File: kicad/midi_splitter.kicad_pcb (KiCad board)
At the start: 2 copper layers, 96 x 50 mm, 44 parts, among them J1 DIN-5_180degree, J2 DIN-5_180degree, J3 DIN-5_180degree, J4 DIN-5_180degree, J5 DIN-5_180degree, J6 Barrel_Jack_Switch, J7 DIN-5_180degree, Q1 BC817, U1 6N138, U2 74LS14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

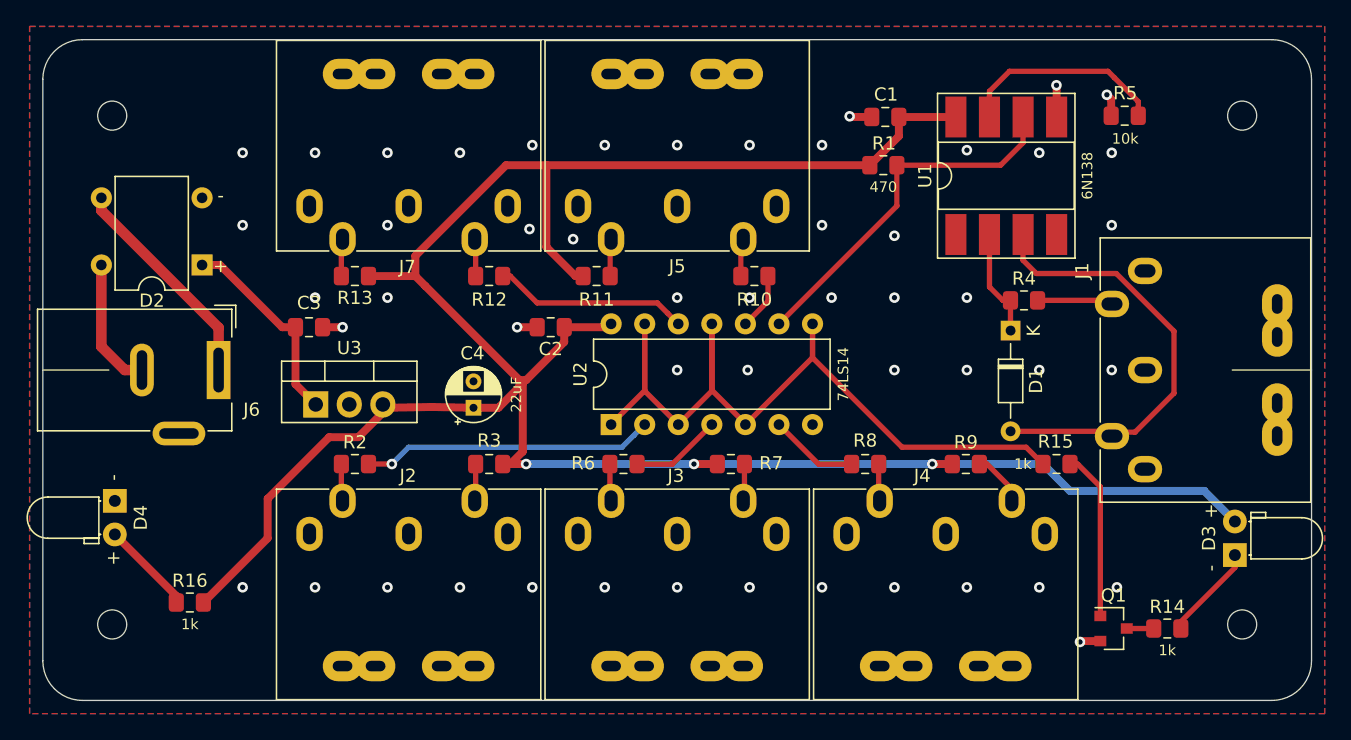
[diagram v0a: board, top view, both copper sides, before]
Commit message: Adding 6th MIDI OUT and USB power input.
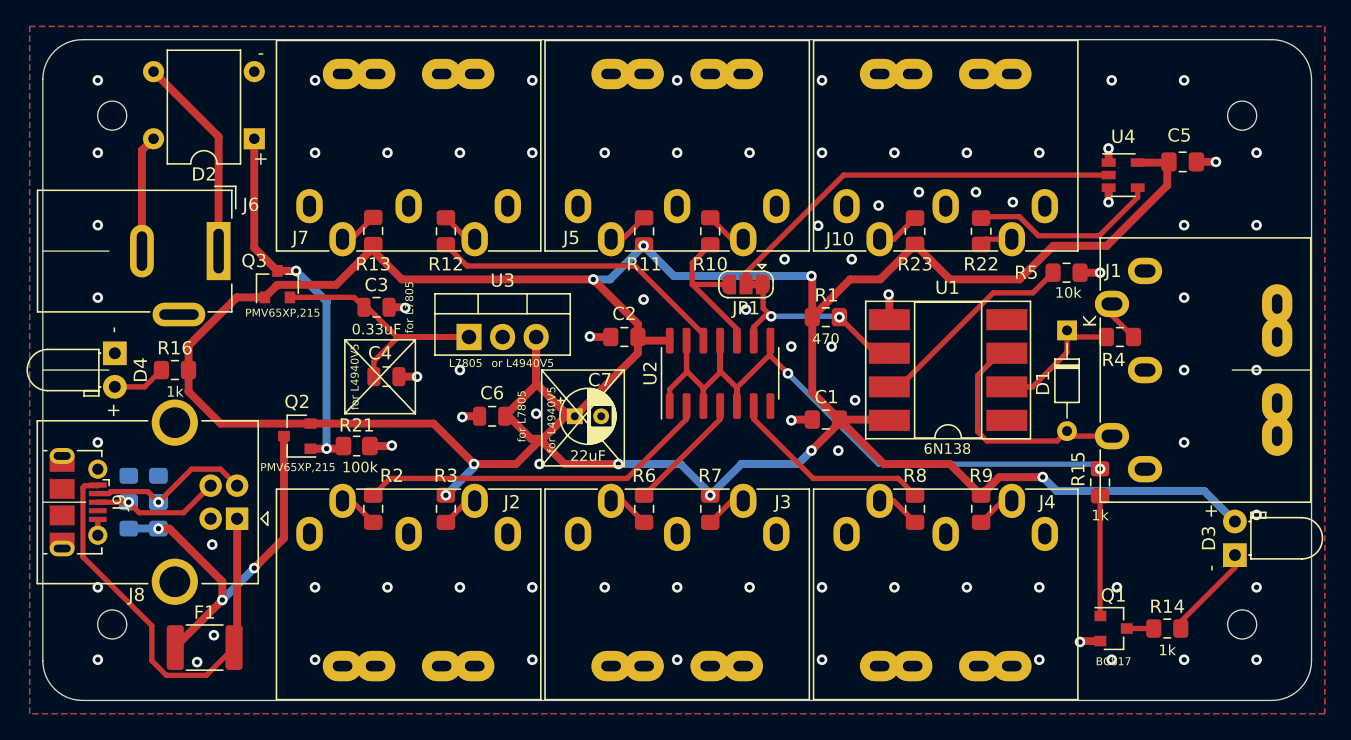
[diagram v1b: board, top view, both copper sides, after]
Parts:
- removed the G*** at (136.7, 116.0)
- removed the G*** at (175.8, 97.4)
- added C5: 0.1uF, Capacitor_SMD:C_0805_2012Metric_Pad1.18x1.45mm_HandSolder, F.Cu at (186.2, 99.2)
- added C6: 0.1uF, Capacitor_SMD:C_0805_2012Metric, F.Cu at (134.0, 118.5)
- added C7: 22uF, Capacitor_THT:CP_Radial_D4.0mm_P2.00mm, F.Cu at (140.2, 118.5)
- added F1: MF-MSMF050-2, Fuse:Fuse_1812_4532Metric_Pad1.30x3.40mm_HandSolder, F.Cu at (112.2, 136.0)
- added G***: LOGO, lib:midi_14mm, B.Cu at (181.8, 96.3)
- added G***: LOGO, lib:x6, B.Cu at (149.8, 114.7)
- added J10: DIN-5_180degree, lib:DIN5MIDI-OOTDTY, F.Cu at (160.8, 102.6)
- added J8: DS1099, Connector_USB:USB_B_OST_USB-B1HSxx_Horizontal, F.Cu at (114.7, 126.2)
- added J9: DS1099, Connector_USB:USB_Micro-B_Molex-105017-0001, F.Cu at (102.7, 125.0)
- added JP1: IN6, Jumper:SolderJumper-3_P1.3mm_Bridged12_RoundedPad1.0x1.5mm, F.Cu at (153.2, 108.5)
- added Q2: PMV65XP,215, Package_TO_SOT_SMD:SOT-23, F.Cu at (119.2, 120.0)
- added Q3: PMV65XP,215, Package_TO_SOT_SMD:SOT-23, F.Cu at (117.8, 108.5)
- added R17: 10k, Resistor_SMD:R_0805_2012Metric_Pad1.20x1.40mm_HandSolder, B.Cu at (106.5, 126.0)
- added R18: 10k, Resistor_SMD:R_0805_2012Metric_Pad1.20x1.40mm_HandSolder, B.Cu at (108.8, 126.0)
- added R19: 10k, Resistor_SMD:R_0805_2012Metric_Pad1.20x1.40mm_HandSolder, B.Cu at (106.5, 124.0)
- added R20: 10k, Resistor_SMD:R_0805_2012Metric_Pad1.20x1.40mm_HandSolder, B.Cu at (108.8, 124.0)
- added R21: 100k, Resistor_SMD:R_0805_2012Metric_Pad1.20x1.40mm_HandSolder, F.Cu at (123.8, 120.8)
- added R22: 220, Resistor_SMD:R_0805_2012Metric_Pad1.20x1.40mm_HandSolder, F.Cu at (171.0, 104.5)
- added R23: 220, Resistor_SMD:R_0805_2012Metric_Pad1.20x1.40mm_HandSolder, F.Cu at (166.0, 104.5)
- added U4: 74AUC1G125, Package_TO_SOT_SMD:SOT-23-5, F.Cu at (181.8, 100.2)
- C3: value 0.1uF -> 0.33uF; footprint Capacitor_SMD:C_0805_2012Metric_Pad1.15x1.40mm_HandSolder -> Capacitor_SMD:C_0805_2012Metric
- C4: value 22uF -> 0.1uF; footprint Capacitor_THT:CP_Radial_D4.0mm_P2.00mm -> Capacitor_SMD:C_0805_2012Metric
- U2: value 74LS14 -> 74HC14D; footprint Package_DIP:DIP-14_W7.62mm -> Package_SO:SOIC-14_3.9x8.7mm_P1.27mm
- U3: value LF50_TO220 -> L7805
- moved C1 23.3 mm to (159.2, 118.8)
- moved R16 17.6 mm to (110.0, 115.0)
- moved U1 15.3 mm to (168.5, 115.0), turned to 180 degrees
- moved U3 12.7 mm to (132.2, 112.5)
- moved R5 12.7 mm to (177.5, 107.6), turned to 0 degrees
- moved R1 12.3 mm to (159.2, 111.0)
- moved REF** 11.9 mm to (115.0, 115.0)
- moved D4 11.2 mm to (105.5, 113.7)
- moved D2 10.3 mm to (116.0, 97.5)
- moved U2 9.11 mm to (151.2, 115.2)
- moved J6 9.00 mm to (113.3, 106.0)
- moved R4 7.77 mm to (181.5, 112.5)
- moved C4 7.00 mm to (126.0, 115.5), turned to 0 degrees
- moved C2 5.62 mm to (144.0, 112.5)
- moved C3 5.33 mm to (125.2, 110.2)
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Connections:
- net Net-(R10-Pad2) renamed OUT5
- C3 pad 1: +9V -> Net-(C3-Pad1)
- C4 pad 1: +5V -> Net-(C3-Pad1)
- U3 pad 1: +9V -> Net-(C3-Pad1)
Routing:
- net +5V: track 183.0 -> 242.4 mm, vias 3 -> 9
- net Net-(F1-Pad2): track 0.00 -> 33.9 mm
- net IN6: track 0.00 -> 31.4 mm
- net VBUS: track 0.00 -> 29.5 mm, vias 0 -> 3
- net Net-(C3-Pad1): track 0.00 -> 23.9 mm
- net Net-(D1-Pad2): track 33.9 -> 18.1 mm
- net Net-(R22-Pad2): track 0.00 -> 14.4 mm
- net +9V: track 15.5 -> 29.1 mm, vias 0 -> 2
- net D-: track 0.00 -> 12.5 mm, vias 0 -> 1
- net RX: track 27.9 -> 15.4 mm, vias 0 -> 2
- net ~RX: track 67.7 -> 57.5 mm, vias 0 -> 2
- net D+: track 0.00 -> 9.72 mm, vias 0 -> 1
- net GND: track 10.4 -> 19.8 mm, vias 51 -> 84
- net Net-(R8-Pad2): track 6.73 -> 15.6 mm
- net Net-(R12-Pad2): track 14.8 -> 22.8 mm
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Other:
- board text added: "2021.01.21"
- board text removed: "2020.09.12"

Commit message: Updating U4 in generated files.
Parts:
- U4: value 74AUC1G125 -> SN74LVC1G125

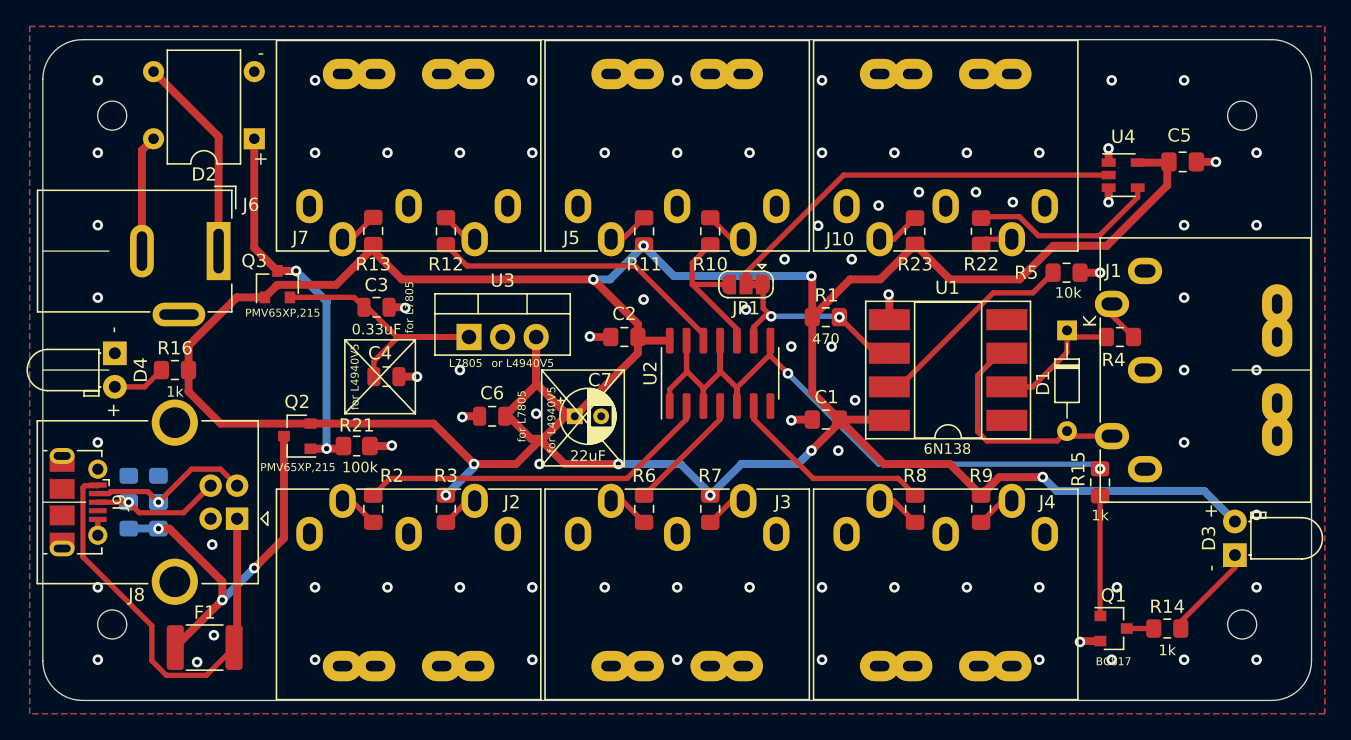
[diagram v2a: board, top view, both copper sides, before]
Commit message: Reducing number of components.
- removing 9-12v power supply option;
- replacing 74hc14 with 74hc540;
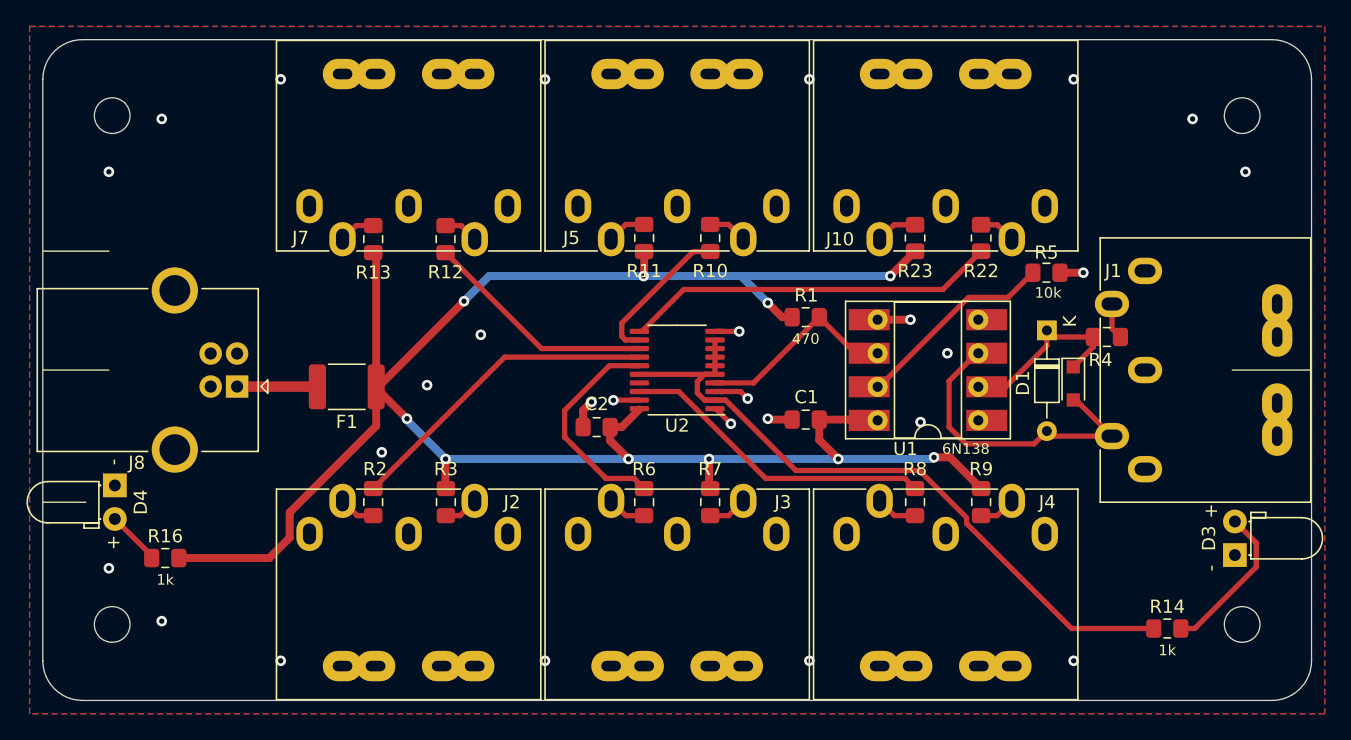
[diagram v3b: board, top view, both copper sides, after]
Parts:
- removed C3: 0.33uF, Capacitor_SMD:C_0805_2012Metric
- removed C4, C6: 0.1uF, Capacitor_SMD:C_0805_2012Metric
- removed C5: 0.1uF, Capacitor_SMD:C_0805_2012Metric_Pad1.18x1.45mm_HandSolder
- removed C7: 22uF, Capacitor_THT:CP_Radial_D4.0mm_P2.00mm
- removed the G*** at (181.8, 96.3)
- removed J6: Barrel_Jack_Switch, Connector_BarrelJack:BarrelJack_Wuerth_6941xx301002
- removed J9: DS1099, Connector_USB:USB_Micro-B_Molex-105017-0001
- removed JP1: IN6, Jumper:SolderJumper-3_P1.3mm_Bridged12_RoundedPad1.0x1.5mm
- removed Q1: BC817, Package_TO_SOT_SMD:SOT-23
- removed Q2, Q3: PMV65XP,215, Package_TO_SOT_SMD:SOT-23
- removed R15: 1k, Resistor_SMD:R_0805_2012Metric_Pad1.15x1.40mm_HandSolder
- removed R17, R18, R19, R20: 10k, Resistor_SMD:R_0805_2012Metric_Pad1.20x1.40mm_HandSolder
- removed R21: 100k, Resistor_SMD:R_0805_2012Metric_Pad1.20x1.40mm_HandSolder
- removed U3: L7805, Package_TO_SOT_THT:TO-220-3_Vertical
- removed U4: SN74LVC1G125, Package_TO_SOT_SMD:SOT-23-5
- D2: value D_Bridge_+-AA -> BAS316.115; footprint Diode_THT:Diode_Bridge_DIP-4_W7.62mm_P5.08mm -> Diode_SMD:D_SOD-323_HandSoldering
- H1, H2, H3, H4: footprint MountingHole:MountingHole_2.2mm_M2_ISO7380 -> MountingHole:MountingHole_2.7mm_M2.5_ISO14580
- U2: value 74HC14D -> MM74HC540MTCX; footprint Package_SO:SOIC-14_3.9x8.7mm_P1.27mm -> Package_SO:TSSOP-20_4.4x6.5mm_P0.65mm
- moved D2 64.7 mm to (178.0, 116.0), turned to 270 degrees
- moved F1 22.5 mm to (123.0, 116.3), turned to 180 degrees
- moved R16 14.2 mm to (109.3, 129.2)
- moved D4 10.0 mm to (105.5, 123.7)
- moved J8 10.0 mm to (114.7, 116.2)
- moved REF** 10.0 mm to (115.0, 125.0)
- moved G*** 7.98 mm to (142.0, 116.7)
- moved C2 7.13 mm to (141.9, 119.3)
- moved U2 3.26 mm to (148.0, 115.0), turned to 180 degrees
- moved C1 1.52 mm to (157.7, 118.8)
- moved D1 1.52 mm to (176.0, 112.0)
- moved R1 1.52 mm to (157.7, 111.0)
- moved R5 1.52 mm to (175.9, 107.6)
- moved U1 1.52 mm to (167.0, 115.0)
- moved R4 0.99 mm to (180.5, 112.5)
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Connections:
- D1 pad 1: Net-(D1-Pad1) -> DK
- D1 pad 2: Net-(D1-Pad2) -> DA
- D2 pad 1: +9V -> DK
- D2 pad 2: GND -> DA
- D3 pad 1: Net-(D3-Pad1) -> GND
- D3 pad 2: +5V -> Net-(D3-Pad2)
- F1 pad 1: VBUS -> +5V
- J1 pad 5: Net-(D1-Pad2) -> DA
- R12 pad 2: Net-(R12-Pad2) -> OUT4
- R14 pad 1: Net-(Q1-Pad3) -> ~RX
- R14 pad 2: Net-(D3-Pad1) -> Net-(D3-Pad2)
- R2 pad 2: Net-(R2-Pad2) -> OUT1
- R22 pad 1: Net-(J10-Pad5) -> OUT6
- R22 pad 2: Net-(R22-Pad2) -> Net-(J10-Pad5)
- R4 pad 1: Net-(D1-Pad1) -> DK
- R6 pad 2: Net-(R6-Pad2) -> OUT2
- R8 pad 2: Net-(R8-Pad2) -> OUT3
- U1 pad 2: Net-(D1-Pad1) -> DK
- U1 pad 3: Net-(D1-Pad2) -> DA
- U2 pad 1: ~RX -> GND
- U2 pad 10: OUT5 -> GND
- U2 pad 11: ~RX -> OUT6
- U2 pad 12: Net-(R12-Pad2) -> OUT5
- U2 pad 13: ~RX -> OUT4
- U2 pad 14: +5V -> OUT1
- U2 pad 2: Net-(R2-Pad2) -> ~RX
- U2 pad 3: ~RX -> GND
- U2 pad 4: Net-(R6-Pad2) -> RX
- U2 pad 6: Net-(R8-Pad2) -> ~RX
- U2 pad 7: GND -> ~RX
- U2 pad 9: RX -> ~RX
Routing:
- net +5V: track 242.4 -> 152.4 mm, vias 9 -> 10
- net IN6: track 31.4 -> 0.00 mm
- net VBUS: track 29.5 -> 0.00 mm, vias 3 -> 0
- net +9V: track 29.1 -> 0.00 mm, vias 2 -> 0
- net OUT6: track 0.00 -> 28.4 mm
- net Net-(F1-Pad2): track 33.9 -> 6.08 mm
- net Net-(R2-Pad2): track 27.1 -> 0.00 mm
- net DA: track 0.00 -> 24.7 mm
- net OUT1: track 0.00 -> 24.3 mm
- net Net-(C3-Pad1): track 23.9 -> 0.00 mm
- net OUT3: track 0.00 -> 23.9 mm
- net Net-(R12-Pad2): track 22.8 -> 0.00 mm
- net Net-(D1-Pad2): track 18.1 -> 0.00 mm
- net OUT4: track 0.00 -> 17.7 mm
- net OUT2: track 0.00 -> 16.7 mm
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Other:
- board text added: "2022.03.21"
- board text removed: "2021.01.21"
